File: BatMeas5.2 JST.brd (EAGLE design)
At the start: 65.1 x 34.3 mm, 50 parts, among them IC1 ATTINY24, IC2 3V3, IC3 3V, J3 BM03B-PASS-1-TFT_(LF)(SN), J4 BM05B-PASS-1-TFT_(LF)(SN)SMD, T1 MMUN2233, T2 MMUN2233, T3 MMUN2233, T4 MMUN2111LT1G, T5 MMUN2111LT1G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

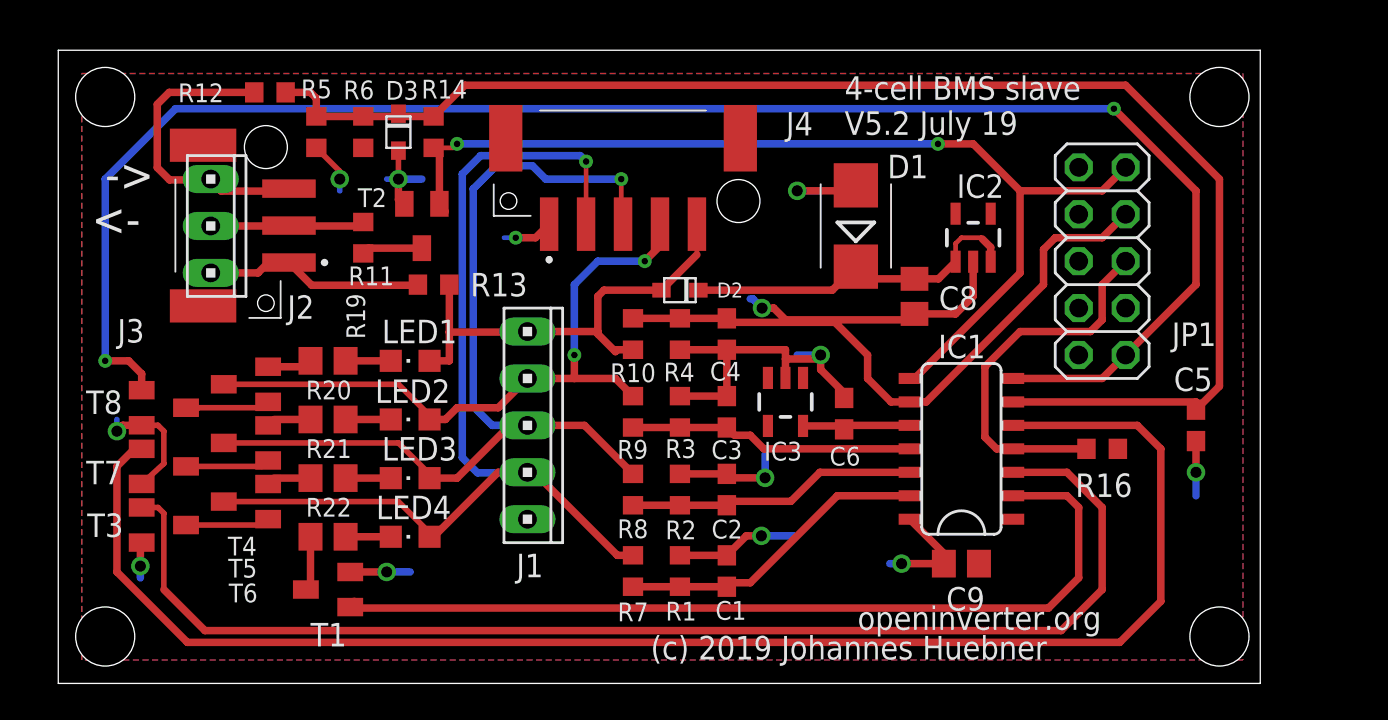
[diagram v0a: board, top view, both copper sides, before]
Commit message: Enlarged board to space new connectors
Enlarged board, now 35x70mm.  Moved bottom tracks other than ground plane to top side.  Holes spaced 2.5mm in from edge of PCB (was 2.54mm)
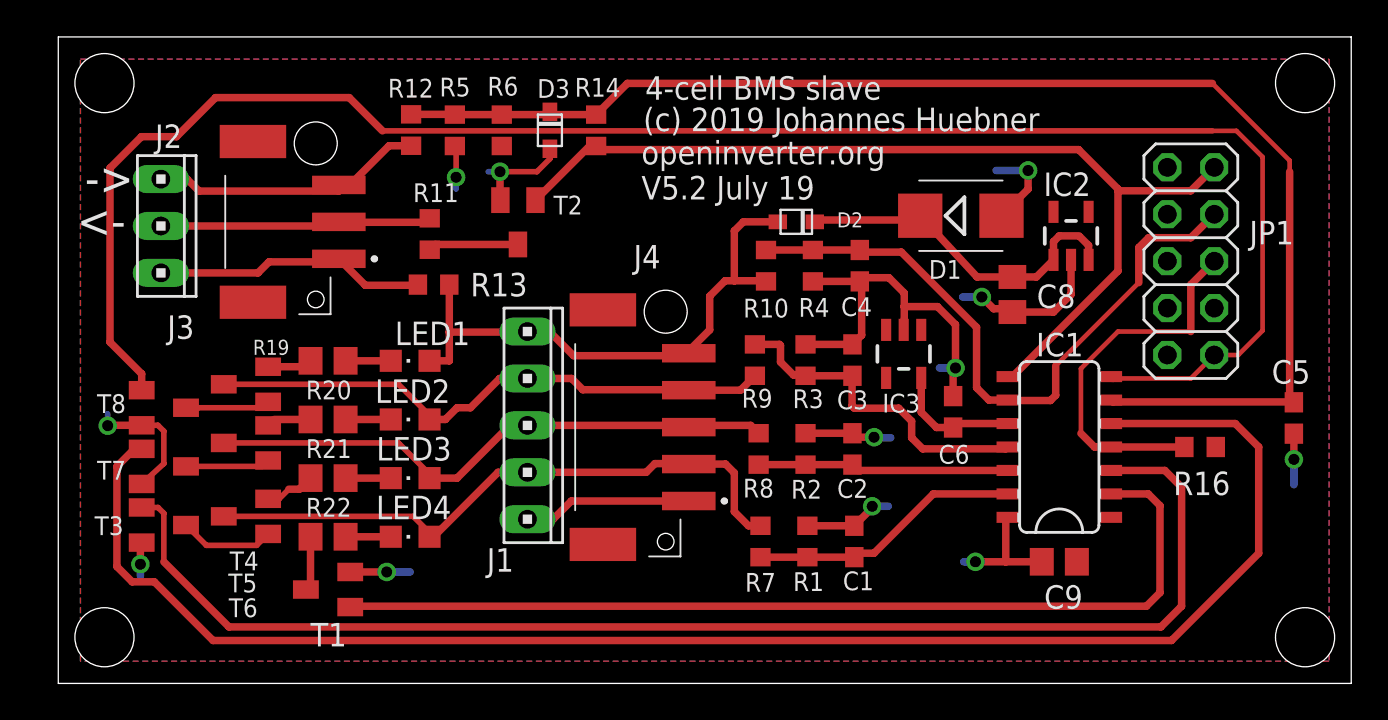
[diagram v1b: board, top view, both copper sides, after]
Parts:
- moved J4 16.3 mm to (31.1, 11.9), turned to 270 degrees
- moved R14 8.80 mm to (29.1, 29.9)
- moved D3 8.20 mm to (26.6, 29.9)
- moved C4 8.10 mm to (43.4, 22.6)
- moved R10 8.10 mm to (38.3, 22.6)
- moved R4 8.10 mm to (40.9, 22.6)
- moved R12 7.91 mm to (19.1, 30.0), turned to 270 degrees
- moved R6 7.50 mm to (24.0, 29.9)
- moved R5 7.50 mm to (21.5, 29.9)
- moved C3 7.35 mm to (43.0, 17.5)
- moved R3 7.35 mm to (40.5, 17.5)
- moved D2 7.31 mm to (40.0, 25.0)
- moved R9 7.17 mm to (37.7, 17.5), turned to 270 degrees
- moved R8 7.15 mm to (37.9, 12.7)
- moved C2 7.15 mm to (43.0, 12.7)
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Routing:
- net N$25: track 56.3 -> 33.9 mm, vias 1 -> 0
- net N$24: track 51.9 -> 31.4 mm, vias 1 -> 0
- net TX: track 8.38 -> 14.7 mm
- net N$17: track 25.6 -> 31.1 mm
- net N$23: track 36.2 -> 31.2 mm, vias 2 -> 0
- net ICP: track 77.9 -> 73.3 mm
- net MOSI: track 92.6 -> 96.8 mm, vias 2 -> 0
- net MISO/INHIBIT: track 55.9 -> 52.2 mm, vias 2 -> 0
- net N$3: track 48.1 -> 51.8 mm
- net N$10: track 83.2 -> 86.9 mm
- net N$4: track 68.2 -> 71.6 mm
- net N$12: track 12.0 -> 14.8 mm
- net VBAT3: track 15.5 -> 18.1 mm
- net VBAT1: track 17.0 -> 14.8 mm
- net VBAT2: track 15.7 -> 13.6 mm
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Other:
- board size 65.1 x 34.3 mm -> 70 x 35 mm

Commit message: Minor updates and added maunfacturing files
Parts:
- D3: value (none) -> MM3Z3V0ST1G
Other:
- board text added: "(c) 2019 J Huebner / A Martell"
- board text removed: "(c) 2019 Johannes Huebner"
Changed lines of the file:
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@@
 <text x="3.645" y="25.935" size="1.778" layer="25" rot="R180">&lt;-</text>
 <text x="31.77" y="31.6" size="1.27" layer="25" font="vector">4-cell BMS slave</text>
-<text x="31.67" y="29.9" size="1.27" layer="25" font="vector">(c) 2019 Johannes Huebner</text>
+<text x="31.67" y="29.9" size="1.27" layer="25" font="vector">(c) 2019 J Huebner / A Martell</text>
 <text x="31.57" y="26.2" size="1.27" layer="25" font="vector">V5.2 July 19</text>
 </plain>
@@
 <attribute name="VALUE" x="37.855" y="23.29" size="0.8128" layer="27" font="vector"/>
 </element>
-<element name="D3" library="adafruit" package="SOD-323F" value="" x="26.615" y="29.945" smashed="yes" rot="R90">
+<element name="D3" library="adafruit" package="SOD-323F" value="MM3Z3V0ST1G " x="26.615" y="29.945" smashed="yes" rot="R90">
 <attribute name="NAME" x="27.695" y="32.717" size="1.016" layer="25" font="vector" rot="R180"/>
 <attribute name="VALUE" x="28.315" y="27.845" size="0.8128" layer="27" font="vector" rot="R90"/>
